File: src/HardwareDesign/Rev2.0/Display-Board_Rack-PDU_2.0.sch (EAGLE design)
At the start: 59 parts, among them IC2 MCP23017-E/ML, T1 BSS138

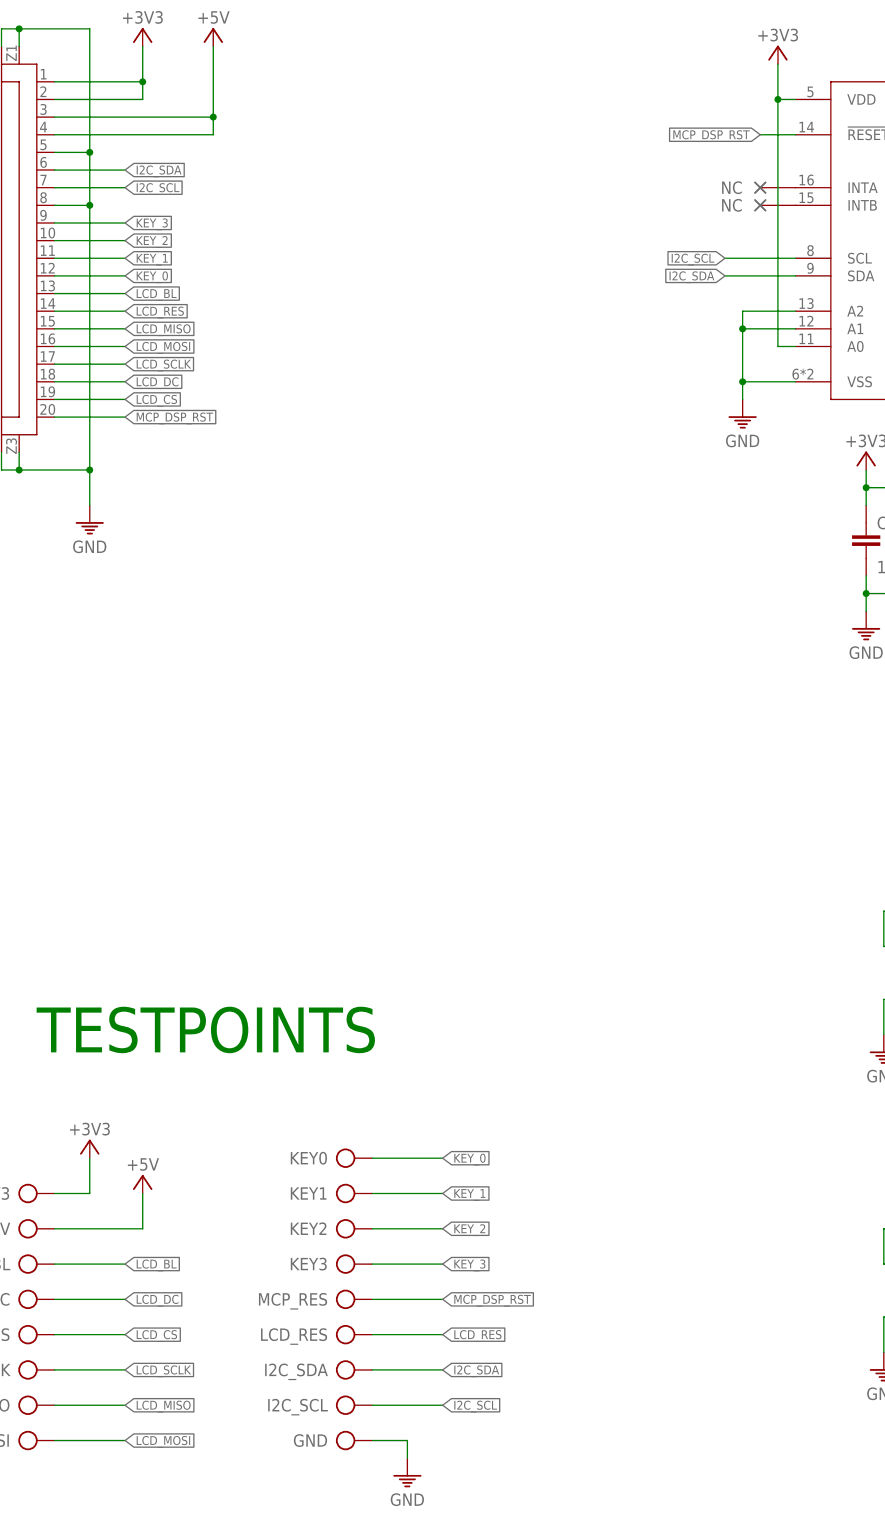
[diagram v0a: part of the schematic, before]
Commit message: source code - pre version. Never RP2040 or any RP series ever. Copiling to this is nightmare
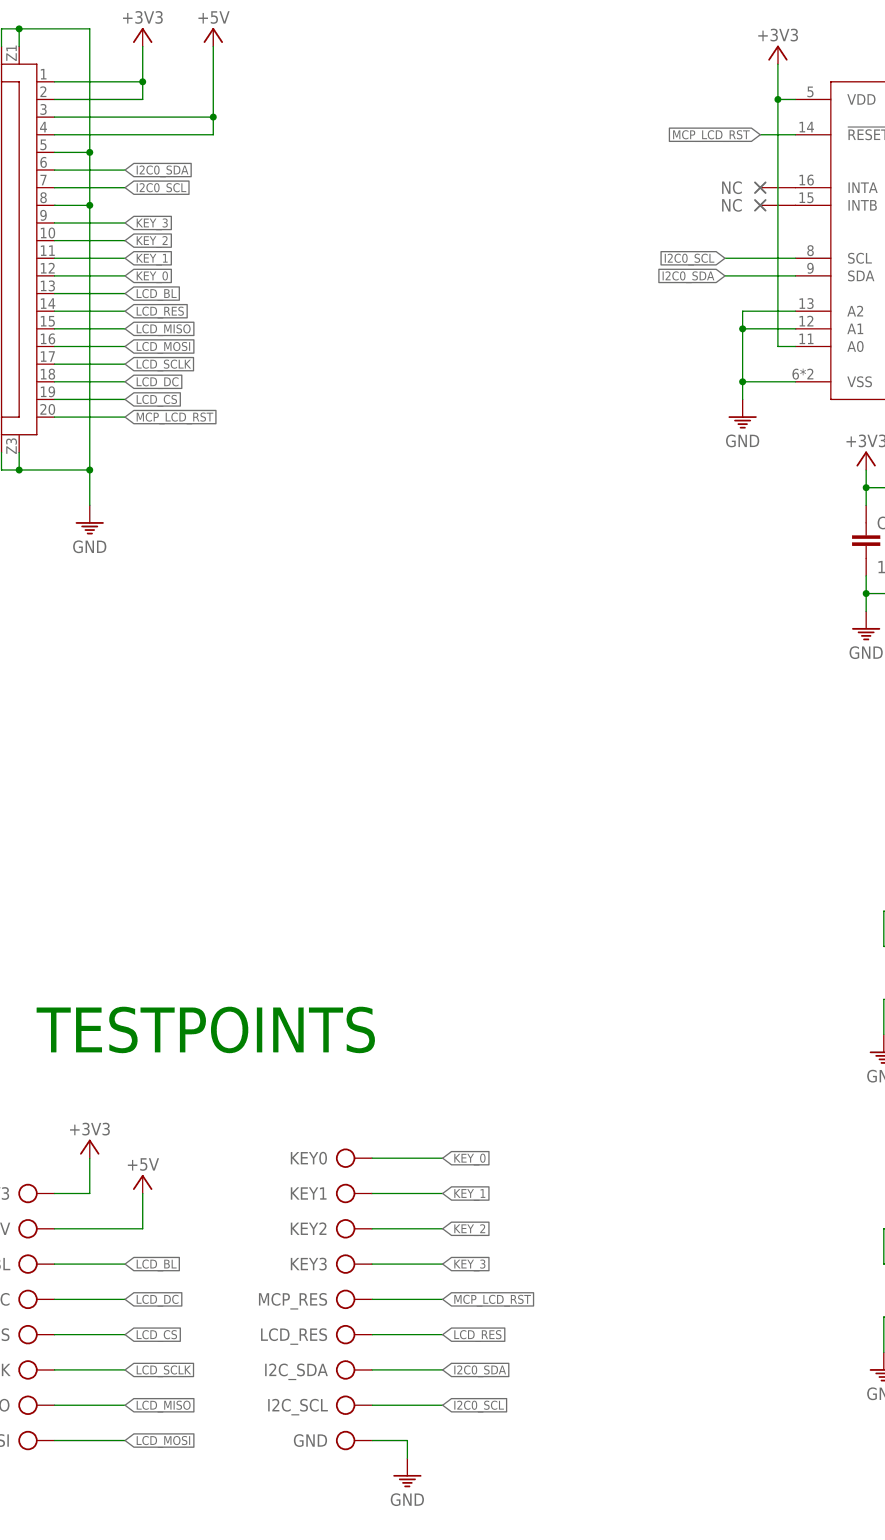
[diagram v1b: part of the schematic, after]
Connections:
- net I2C_SCL renamed I2C0_SCL
- net I2C_SDA renamed I2C0_SDA
- net MCP_DSP_RST renamed MCP_LCD_RST
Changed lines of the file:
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@@
 </segment>
 </net>
-<net name="I2C_SDA" class="0">
+<net name="I2C0_SDA" class="0">
 <segment>
 <wire x1="132.08" y1="210.82" x2="142.24" y2="210.82" width="0.1524" layer="91"/>
@@
 </segment>
 </net>
-<net name="I2C_SCL" class="0">
+<net name="I2C0_SCL" class="0">
 <segment>
 <wire x1="142.24" y1="208.28" x2="132.08" y2="208.28" width="0.1524" layer="91"/>
@@
 </segment>
 </net>
-<net name="MCP_DSP_RST" class="0">
+<net name="MCP_LCD_RST" class="0">
 <segment>
 <wire x1="238.76" y1="215.9" x2="233.68" y2="215.9" width="0.1524" layer="91"/>
